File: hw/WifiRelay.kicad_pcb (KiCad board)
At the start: 2 copper layers, 94 x 54 mm, 38 parts, among them J1 CONN_01X02, J2 CONN_01X06, J3 CONN_01X02, J4 CONN_01X02, K1 G5Q-1A DC5, K2 G5Q-1A DC5, Q1 MMSS8050-H, Q2 MMSS8050-H, SW1 SW_Push, SW2 SW_Push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

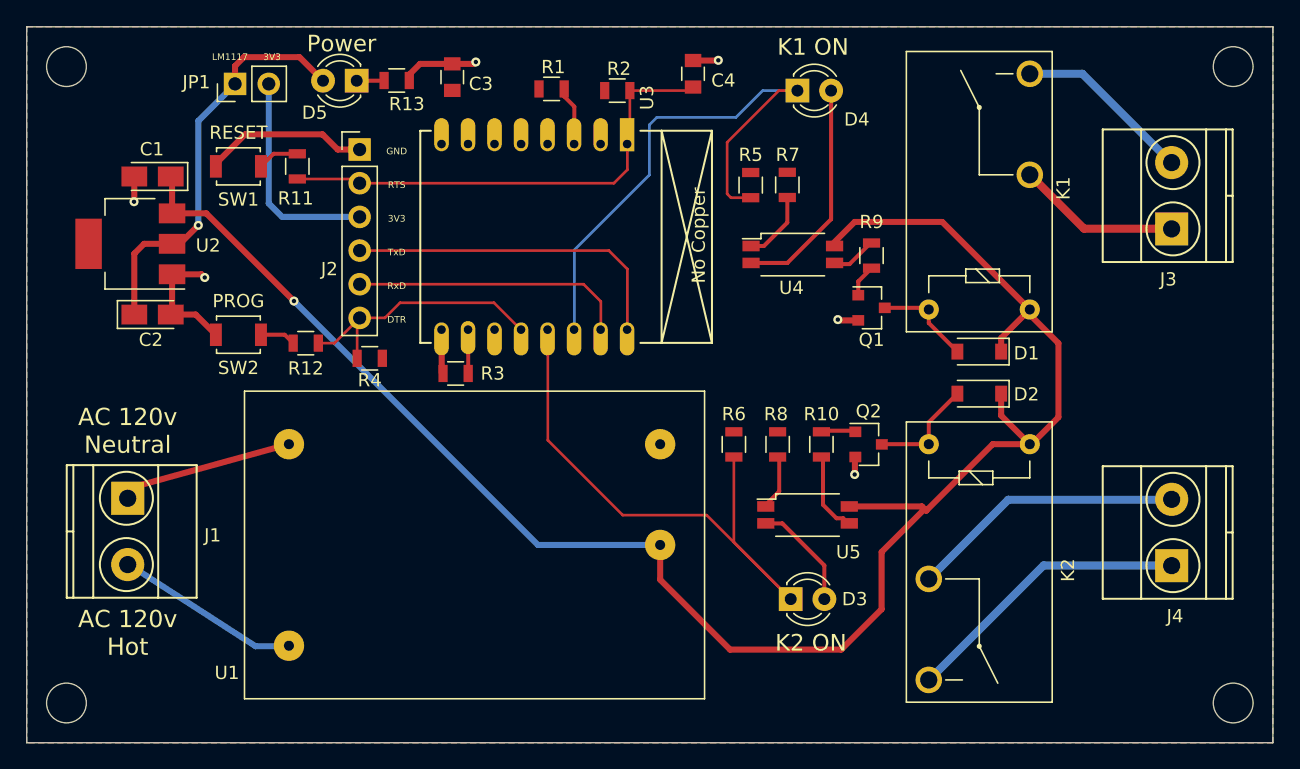
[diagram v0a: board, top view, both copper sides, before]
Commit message: V1.1 hardware with low cost components Dropped LEDs Added +5v test point Changed two single optos for 1 dual Changed relay, +5v AC/DC conv, and 100uF parts footprints
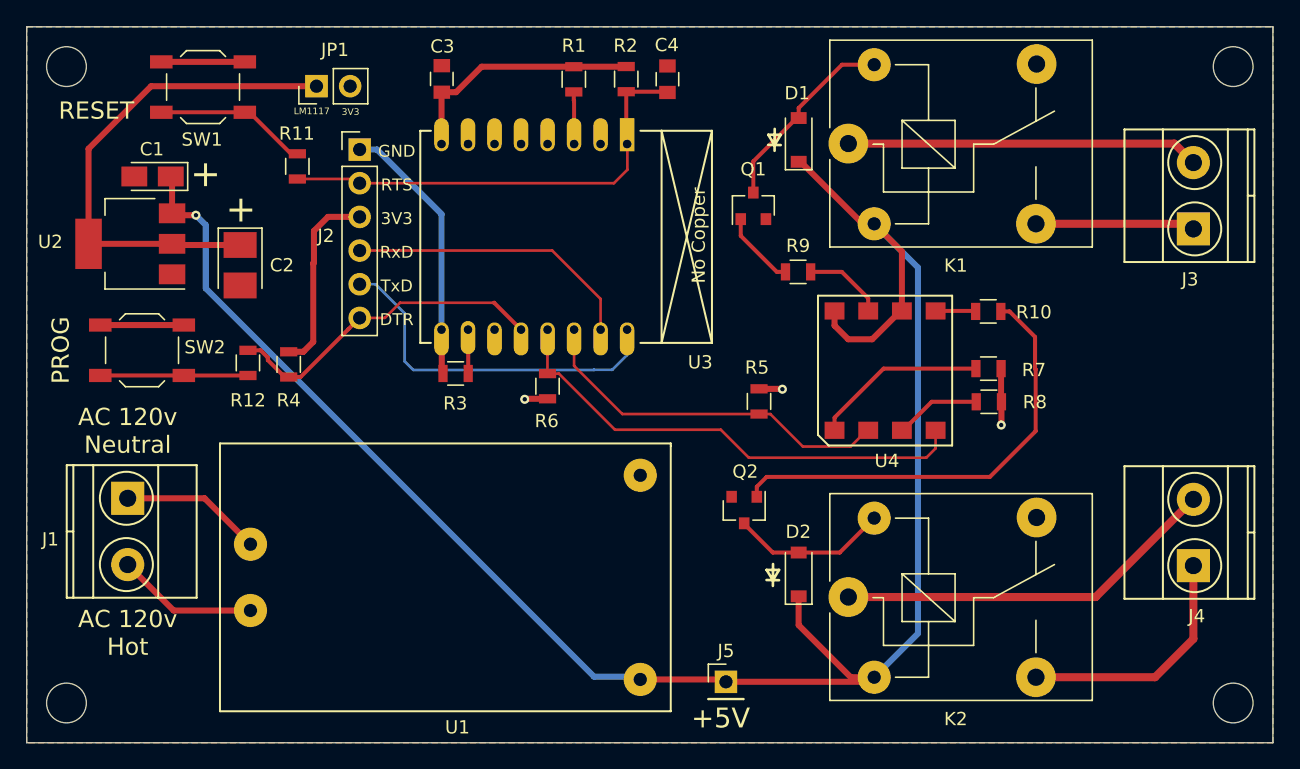
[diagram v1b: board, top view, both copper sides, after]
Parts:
- removed D3, D4, D5: LED, LEDs:LED_D3.0mm
- removed R13: 1K, Resistors_SMD:R_0805
- removed U5: TCMT1100, Housings_SSOP:SOP-4_4.4x2.8mm_Pitch1.27mm
- added J5: TEST_1P, Pin_Headers:Pin_Header_Straight_1x01_Pitch2.54mm, F.Cu at (110.8, 125.1)
- C2: footprint Capacitors_Tantalum_SMD:CP_Tantalum_Case-A_EIA-3216-18_Reflow -> Capacitors_Tantalum_SMD:CP_Tantalum_Case-B_EIA-3528-21_Reflow
- K1, K2: value G5Q-1A DC5 -> Songle-SRD-05VDC-SL-C; footprint Relays_THT:Relay_SPST-NO_OMRON-G5Q -> Relays_THT:Relay_SPDT_SANYOU_SRD_Series_Form_C
- SW1, SW2: footprint Buttons_Switches_SMD:SW_SPST_B3U-1000P -> Buttons_Switches_SMD:SW_SPST_TL3342
- U1: value IRM-02-5 -> HLK-PM01; footprint Converters_DCDC_ACDC:ACDC-Converter_MeanWell-IRM-02-x -> WifiRelay:HLK-PM01
- U2: footprint TO_SOT_Packages_SMD:SOT-223 -> TO_SOT_Packages_SMD:SOT-223-3Lead_TabPin2
- U4: value TCMT1100 -> PC827; footprint Housings_SSOP:SOP-4_4.4x2.8mm_Pitch1.27mm -> WifiRelay:SOIC-8
- moved D1 21.0 mm to (116.3, 84.2), turned to 90 degrees
- moved R7 20.5 mm to (130.6, 101.5), turned to 0 degrees
- moved D2 19.3 mm to (116.3, 117.0), turned to 90 degrees
- moved K1 18.5 mm to (120.0, 84.5), turned to 0 degrees
- moved R5 16.3 mm to (113.3, 104.0)
- moved R8 16.3 mm to (130.6, 104.0), turned to 0 degrees
- moved R10 16.1 mm to (130.6, 97.2), turned to 180 degrees
- moved U1 15.5 mm to (89.6, 117.2)
- moved R6 14.7 mm to (97.3, 102.8), turned to 90 degrees
- moved K2 13.0 mm to (120.0, 118.7), turned to 0 degrees
- moved Q1 11.8 mm to (112.9, 89.2), turned to 90 degrees
- moved U4 11.2 mm to (122.8, 101.6)
- moved Q2 10.6 mm to (112.2, 112.2), turned to 270 degrees
- moved C2 7.58 mm to (74.1, 93.7), turned to 270 degrees
- moved SW2 7.36 mm to (66.7, 100.1)
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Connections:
- net /DTR renamed /GPIO0
- net /RTS renamed /RESET
- C3 pad 1: +3V3 -> GND
- C3 pad 2: GND -> +3V3
- J2 pad 4: /TXD -> /RXD
- J2 pad 5: /RXD -> /TXD
- K1 pad 1: +5V -> Net-(J3-Pad2)
- K1 pad 2: Net-(J3-Pad1) -> +5V
- K1 pad 3: Net-(J3-Pad2) -> Net-(J3-Pad1)
- K2 pad 1: Net-(D2-Pad2) -> Net-(J4-Pad2)
- K2 pad 2: Net-(J4-Pad2) -> +5V
- K2 pad 5: +5V -> Net-(D2-Pad2)
- U3 pad 11: Net-(U3-Pad11) -> (no net)
- U3 pad 2: Net-(U3-Pad2) -> (no net)
- U3 pad 4: Net-(U3-Pad4) -> (no net)
- U3 pad 5: Net-(U3-Pad5) -> (no net)
- U3 pad 6: Net-(U3-Pad6) -> (no net)
- U3 pad 7: Net-(U3-Pad7) -> (no net)
- U4 pad 2: Net-(D4-Pad2) -> /~RELAY1
- U4 pad 3: Net-(R9-Pad2) -> Net-(R8-Pad1)
- U4 pad 4: +5V -> /~RELAY2
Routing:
- net Net-(Q2-Pad1): track 2.90 -> 34.1 mm
- net +3V3: track 16.3 -> 41.2 mm, vias 0 -> 3
- net Net-(D4-Pad2): track 17.5 -> 0.00 mm
- net /~RELAY1: track 42.8 -> 28.0 mm
- net Net-(J3-Pad2): track 13.6 -> 28.3 mm
- net Net-(R12-Pad1): track 2.69 -> 11.1 mm
- net Net-(R11-Pad2): track 3.14 -> 11.6 mm
- net Net-(D3-Pad2): track 8.35 -> 0.00 mm
- net Net-(J4-Pad2): track 20.8 -> 29.1 mm
- net Net-(R7-Pad1): track 5.36 -> 13.2 mm
- net Net-(D1-Pad2): track 7.44 -> 14.9 mm
- net Net-(C2-Pad1): track 31.2 -> 38.4 mm, vias 1 -> 0
- net +5V: track 136.8 -> 142.6 mm
- net /~RELAY2: track 44.1 -> 38.4 mm
- net GND: track 38.6 -> 34.0 mm, vias 6 -> 0
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- added copper zone on B.Cu, net +3V3
- added copper zone on F.Cu, net GND
- removed copper zone on F.Cu, net +3V3
- removed copper zone on B.Cu, net GND
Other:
- board text added: "+"
- board text added: "+5V"
- board text added: "K1/J3"
- board text added: "K2/J4"
- board text added: "WiFi Controller, v1.1 Jeff Davis, N0DY 5/28/2017"
- board text removed: "K1 ON"
- board text removed: "K1/J1"
- board text removed: "K2 ON"
- board text removed: "K2/J2"
- board text removed: "Power"
- board text removed: "WiFi Pool Light Controller, v1.0 Jeff Davis, N0DY 4/30/2017"
